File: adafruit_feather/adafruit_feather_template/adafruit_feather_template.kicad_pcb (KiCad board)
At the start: 2 copper layers, 50.8 x 22.9 mm, 14 parts, among them J1 4040_Header_Male_Vert_12pin_0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, J2 4039_Header_Male_Vert_16pin_0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, J3 3096_USBC_RA_SMD, Q1 4043_DMG3414_Nch_Mosfet_SOT23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, SW1 RST, U1 4042_MCP73831_Battery_Charger, U2 CRG, U3 PWR, U4 3093_MIC5225_3v3

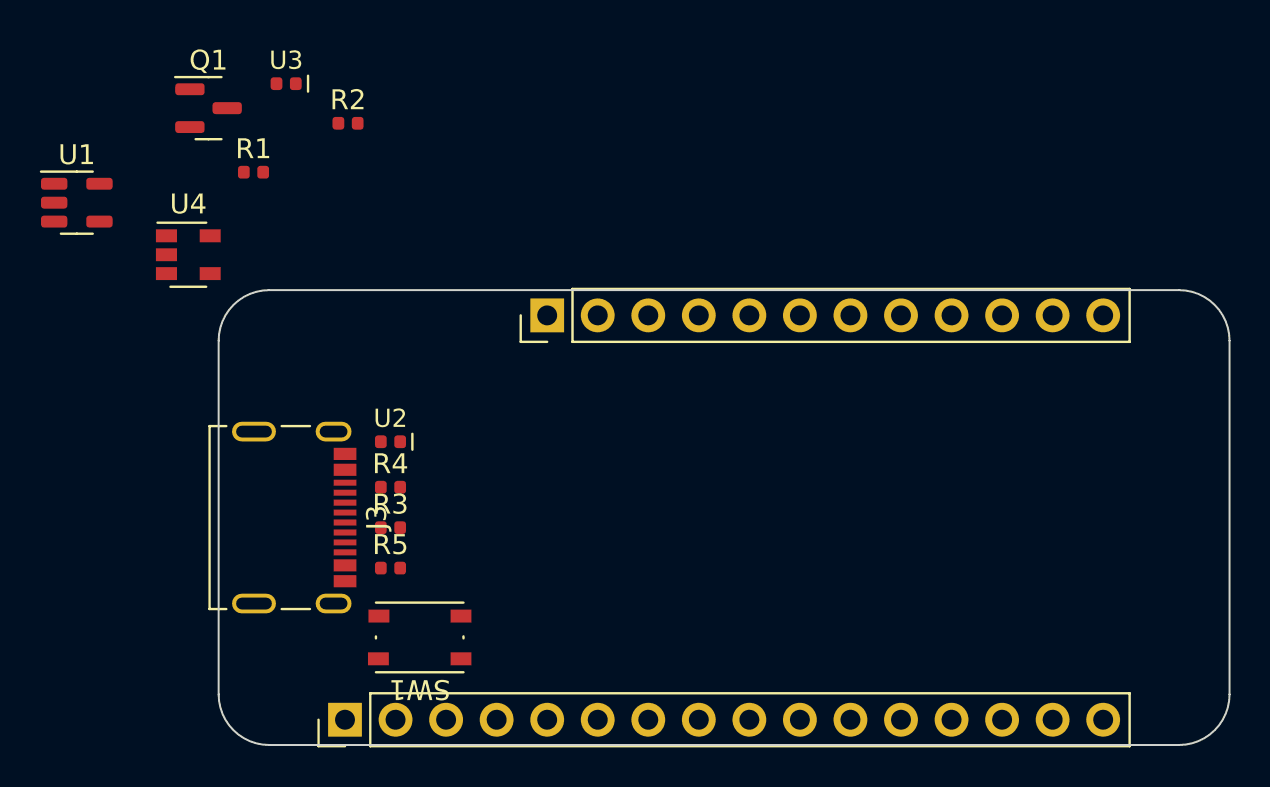
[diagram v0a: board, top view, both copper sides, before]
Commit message: Added some more of the LiPo circuitry, LEDs, and connectors
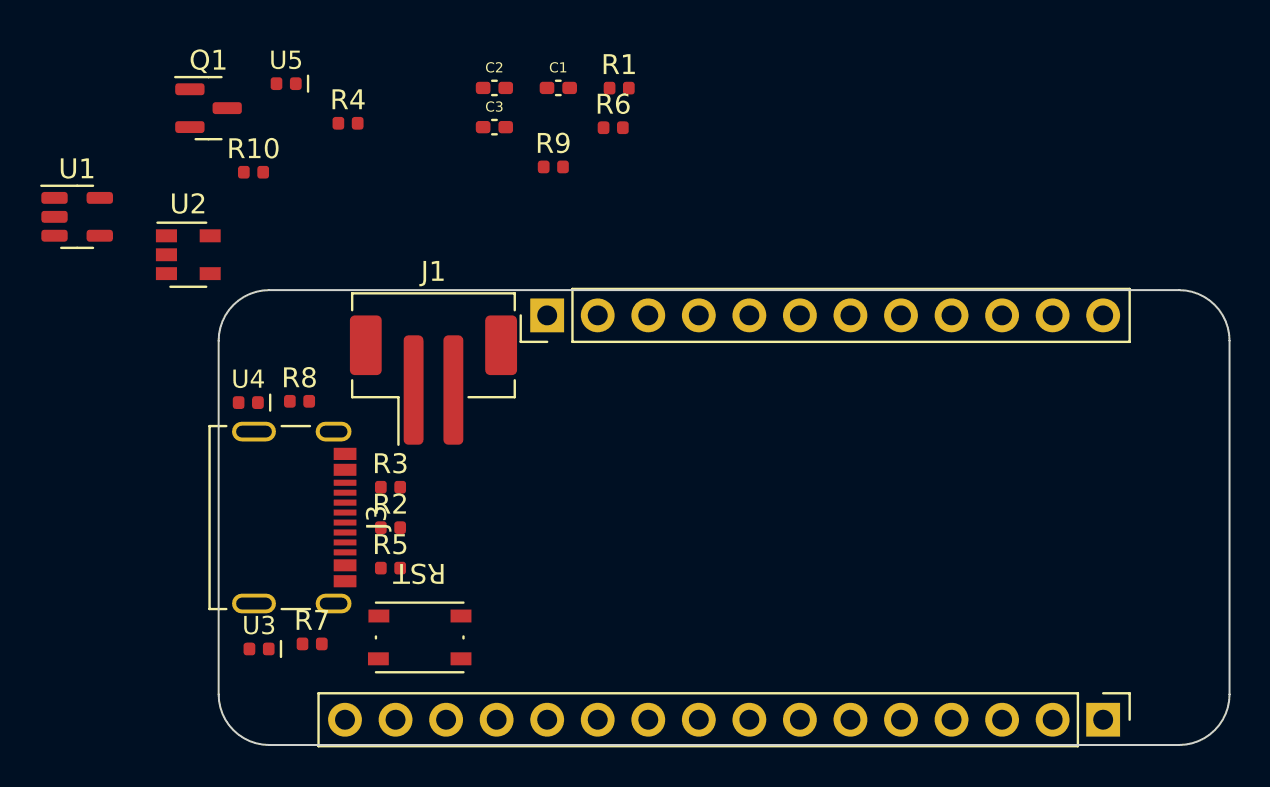
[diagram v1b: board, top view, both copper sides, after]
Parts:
- added C1: 4013_Capacitor_1u_16V_0402, Shulltronics_Generics:C_0402_HandSolder, F.Cu at (149.1, 71.1)
- added C2: 4013_Capacitor_1u_16V_0402, Shulltronics_Generics:C_0402_HandSolder, F.Cu at (145.9, 71.1)
- added C3: 4013_Capacitor_1u_16V_0402, Shulltronics_Generics:C_0402_HandSolder, F.Cu at (145.9, 73.1)
- added J1: 4045_Connector_PH_2pos_RA_SMD, Shulltronics_Connectors:4045_JST_PH_2pos_RA_SMD, F.Cu at (142.9, 85.8)
- added R1: 4017_Resistor_SMD_100k_0.125W_1%_1, Shulltronics_Generics:RES-0402, F.Cu at (152.2, 71.1)
- added R6: 4009_Resistor_SMD_5k1_0.10W_1%, Shulltronics_Generics:RES-0402, F.Cu at (151.9, 73.1)
- added R7: 4038_Resistor_SMD_100_0.125W_1%, Shulltronics_Generics:RES-0402, F.Cu at (136.8, 99.1)
- added R8: 4038_Resistor_SMD_100_0.125W_1%, Shulltronics_Generics:RES-0402, F.Cu at (136.1, 86.9)
- added R9: 4038_Resistor_SMD_100_0.125W_1%, Shulltronics_Generics:RES-0402, F.Cu at (148.9, 75.1)
- added U4: 4044_LED_RED_SMD, Shulltronics_Generics:LED_0402, F.Cu at (133.6, 86.9)
- moved J2 38.1 mm to (176.5, 102.9), turned to -90 degrees
- moved U3 12.3 mm to (134.1, 99.3)
- moved U1 0.71 mm to (125.0, 77.6)
- renumbered J1 to J4, R1 to R10, R3 to R2, R4 to R3, R2 to R4, U4 to U2, U2 to U3, U3 to U5
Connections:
- J2 pad 13: unconnected-(J2-Pad13) -> GND
- J2 pad 14: unconnected-(J2-Pad14) -> /VREF
- J2 pad 15: unconnected-(J2-Pad15) -> VCC
- J2 pad 16: unconnected-(J2-Pad16) -> /~{RST}
- J2 pad 2: unconnected-(J2-Pad2) -> /TX
- J2 pad 3: unconnected-(J2-Pad3) -> /RX
- J2 pad 4: unconnected-(J2-Pad4) -> /MISO
- J2 pad 5: unconnected-(J2-Pad5) -> /MOSI
- J2 pad 6: unconnected-(J2-Pad6) -> /SCK
- J3 pad A1/B12: unconnected-(J3-PadA1/B12) -> GND
- J3 pad A4/B9: unconnected-(J3-PadA4/B9) -> VUSB
- J3 pad A5: unconnected-(J3-PadA5) -> /CC1
- J3 pad A6: unconnected-(J3-PadA6) -> /USB_D+
- J3 pad A7: unconnected-(J3-PadA7) -> /USB_D-
- J3 pad B1/A12: unconnected-(J3-PadB1/A12) -> GND
- J3 pad B4/A9: unconnected-(J3-PadB4/A9) -> VUSB
- J3 pad B5: unconnected-(J3-PadB5) -> /CC2
- J3 pad B6: unconnected-(J3-PadB6) -> /USB_D+
- J3 pad B7: unconnected-(J3-PadB7) -> /USB_D-
- J4 pad 1: unconnected-(J1-Pad1) -> VBAT
- J4 pad 11: unconnected-(J1-Pad11) -> /SCL
- J4 pad 12: unconnected-(J1-Pad12) -> /SDA
- J4 pad 2: unconnected-(J1-Pad2) -> /~{EN}
- J4 pad 3: unconnected-(J1-Pad3) -> VUSB
- Q1 pad 1: unconnected-(Q1-Pad1) -> /~{EN}
- Q1 pad 2: unconnected-(Q1-Pad2) -> GND
- R2 pad 1: unconnected-(R3-Pad1) -> /D+
- R2 pad 2: unconnected-(R3-Pad2) -> /USB_D+
- R3 pad 1: unconnected-(R4-Pad1) -> /D-
- R3 pad 2: unconnected-(R4-Pad2) -> /USB_D-
- R4 pad 1: unconnected-(R2-Pad1) -> /CC1
- R4 pad 2: unconnected-(R2-Pad2) -> GND
- R5 pad 1: unconnected-(R5-Pad1) -> /CC2
- R5 pad 2: unconnected-(R5-Pad2) -> GND
- SW1 pad 1: unconnected-(SW1-Pad1) -> GND
- SW1 pad 2: unconnected-(SW1-Pad2) -> /~{RST}
- U1 pad 1: unconnected-(U1-Pad1) -> Net-(R7-Pad1)
- U1 pad 2: unconnected-(U1-Pad2) -> GND
- U1 pad 3: unconnected-(U1-Pad3) -> VBAT
- U1 pad 4: unconnected-(U1-Pad4) -> VDD
- U1 pad 5: unconnected-(U1-Pad5) -> Net-(R6-Pad1)
- U2 pad 1: unconnected-(U4-Pad1) -> VDD
- U2 pad 2: unconnected-(U4-Pad2) -> GND
- U2 pad 3: unconnected-(U4-Pad3) -> /~{EN}
- U2 pad 5: unconnected-(U4-Pad5) -> VCC
- U3 pad 1: unconnected-(U2-Pad1) -> VDD
- U3 pad 2: unconnected-(U2-Pad2) -> Net-(R7-Pad2)
- U5 pad 1: unconnected-(U3-Pad1) -> Net-(R9-Pad2)
- U5 pad 2: unconnected-(U3-Pad2) -> GND
